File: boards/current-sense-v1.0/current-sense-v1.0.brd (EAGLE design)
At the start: 70.5 x 80.5 mm, 89 parts, among them IC1 ISO7241, IC2 ISO7241, IC3 ISO7242, IC4 ISO7240, J1 4-PIN_2MM-H, J2 MKS-1658, J3 8-PIN_2MM-H, J6 DF22-2, Q1 IRFH7545, Q2 IRFH7545, Q3 IRFH7545, Q4 IRFH7545, Q5 IRFH7545, Q6 IRFH7545, U1 DRV8303DCA, U13 TLV70233DBVR, U2 INA240PWR, U3 INA240PWR, U4 INA240PWR, U6 ADS8028IRTJT, U7 MPM3620GQV-P, U8 VND5E006ASPTR-E, U9 TLV70450

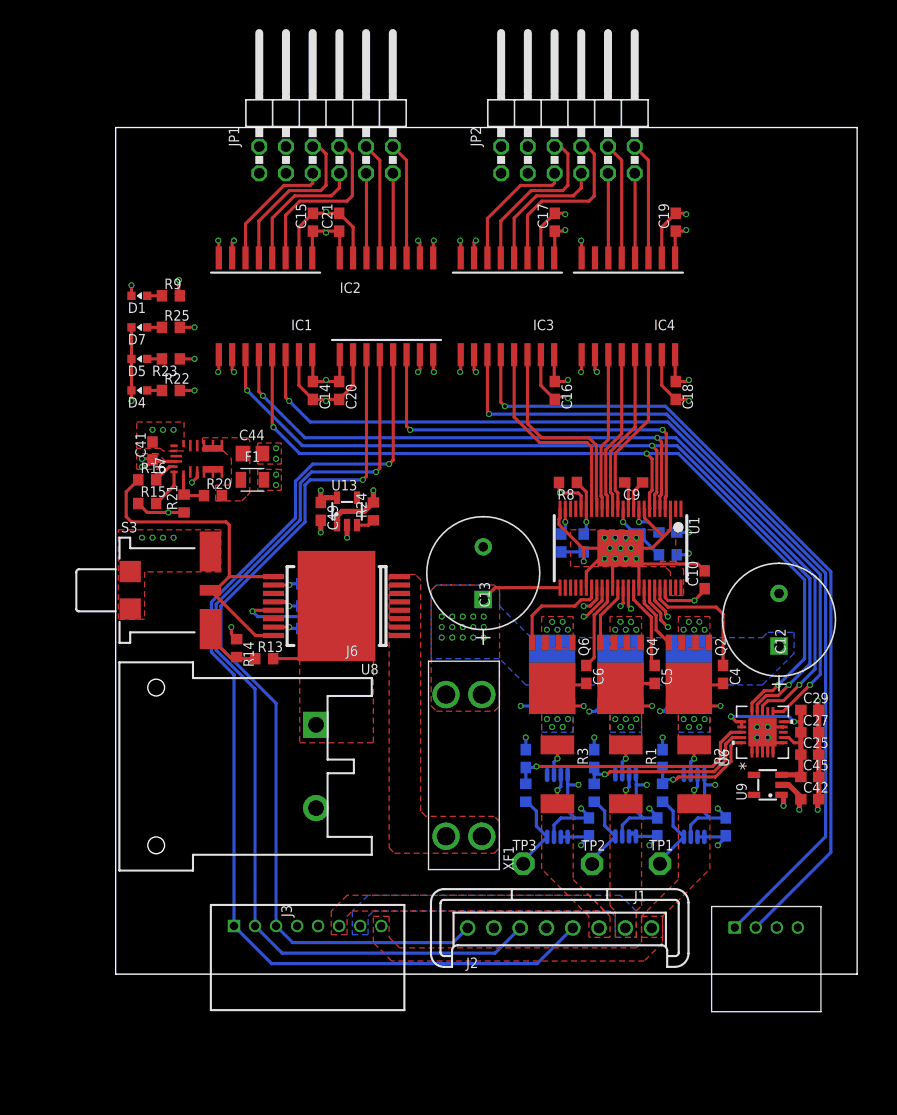
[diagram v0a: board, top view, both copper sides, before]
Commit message: Silkscreen fixes
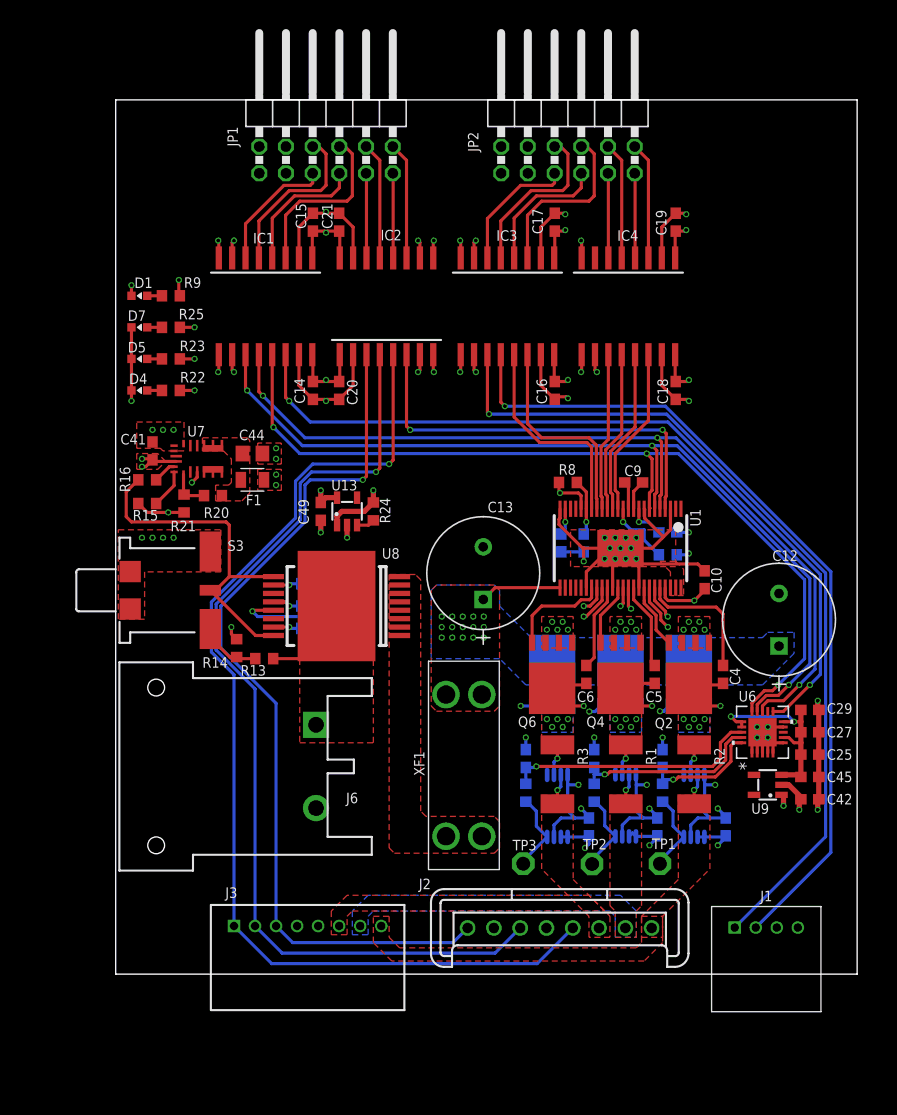
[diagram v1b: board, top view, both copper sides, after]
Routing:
- net +18.5V: track 29.0 -> 17.4 mm
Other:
- board size 70.5 x 80.5 mm -> 70.5 x 83.1 mm

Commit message: rotated the LDO
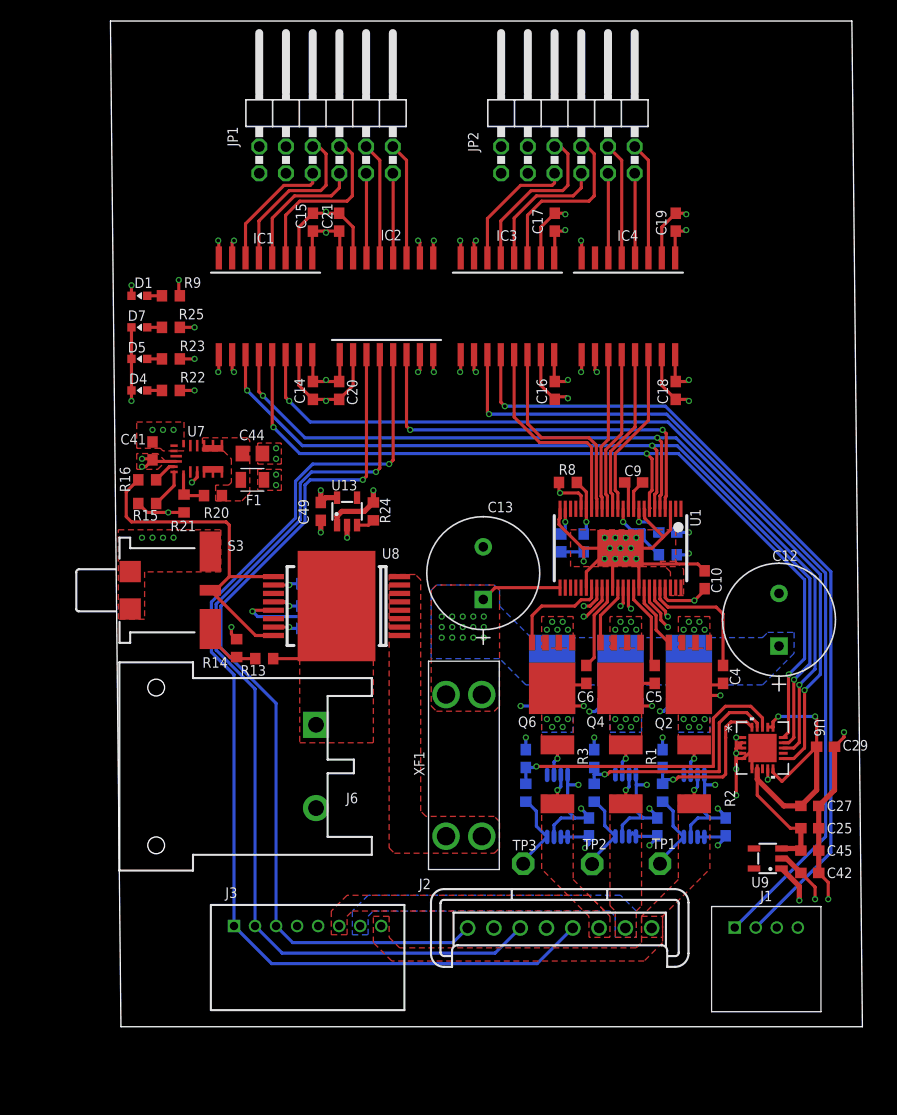
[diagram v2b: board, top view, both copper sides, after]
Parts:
- moved C25 7.00 mm to (66.0, 13.9)
- moved C27 7.00 mm to (66.0, 16.0)
- moved C42 7.00 mm to (66.0, 9.62)
- moved C45 7.00 mm to (66.0, 11.8)
- moved U9 7.00 mm to (62.0, 11.0)
- moved C29 3.81 mm to (67.5, 21.6)
- moved U6 1.50 mm to (61.5, 21.5), turned to 0 degrees
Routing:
- net ADC_5V: track 19.8 -> 35.4 mm, vias 2 -> 1
- net GND: track 183.3 -> 195.8 mm
- net SENSE_C: track 24.3 -> 30.5 mm
- net SENSE_B: track 17.9 -> 23.0 mm
- net CS_ADC: track 77.3 -> 81.4 mm
- net SENSE_A: track 11.4 -> 15.2 mm
- net N$3: track 0.00 -> 3.47 mm, vias 0 -> 1
- net MOSI: track 86.4 -> 88.8 mm
- net +18.5V: track 17.4 -> 19.3 mm
- net MISO: track 86.0 -> 87.6 mm
- net SH_A: track 28.3 -> 26.9 mm
- net SCK: track 84.1 -> 84.9 mm
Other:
- board size 70.5 x 83.1 mm -> 71.5 x 95.6 mm

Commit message: removed two ground symbols from board
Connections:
- net GND: no longer S3.LEG1, S3.LEG3
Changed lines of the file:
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@@
 <contactref element="U8" pad="13"/>
 <contactref element="R14" pad="1"/>
-<contactref element="S3" pad="LEG1"/>
-<contactref element="S3" pad="LEG3"/>
 <contactref element="S3" pad="3"/>
 <contactref element="D4" pad="C"/>
@@
 <wire x1="50.3" y1="43.3507375" x2="52" y2="41.6507375" width="0.3" layer="1"/>
 <wire x1="62" y1="18.5" x2="62.000125" y2="18.500125" width="0.1524" layer="1"/>
-<wire x1="44.305" y1="58.9" x2="51.925" y2="58.9" width="0" layer="19" extent="1-1"/>
-<wire x1="43" y1="54.75" x2="44.25" y2="57.25" width="0" layer="19" extent="1-1"/>
-<wire x1="32.805" y1="58.9" x2="40.425" y2="58.9" width="0" layer="19" extent="1-1"/>
-<wire x1="30.25" y1="57.25" x2="32.75" y2="57.25" width="0" layer="19" extent="1-1"/>
-<wire x1="22.575" y1="58.9" x2="30.195" y2="58.9" width="0" layer="19" extent="1-1"/>
-<wire x1="15.25" y1="50" x2="18.75" y2="54.65" width="0" layer="19" extent="1-1"/>
-<wire x1="15.25" y1="49" x2="15.25" y2="50" width="0" layer="19" extent="1-1"/>
-<wire x1="13.95" y1="49.5" x2="15.25" y2="50" width="0" layer="19" extent="1-1"/>
-<wire x1="7.75" y1="47.75" x2="13.95" y2="49.5" width="0" layer="19" extent="1-1"/>
-<wire x1="6.5" y1="43.9" x2="7.25" y2="46.75" width="0" layer="19" extent="1-1"/>
-<wire x1="5.5" y1="41.5" x2="5" y2="43.9" width="0" layer="19" extent="1-1"/>
-<wire x1="4.5" y1="41.5" x2="5.5" y2="41.5" width="0" layer="19" extent="1-1"/>
-<wire x1="3.5" y1="41.5" x2="4.5" y2="41.5" width="0" layer="19" extent="1-1"/>
-<wire x1="2.5" y1="41.5" x2="3.5" y2="41.5" width="0" layer="19" extent="1-1"/>
-<wire x1="5.55" y1="49.75" x2="7.75" y2="47.75" width="0" layer="19" extent="1-1"/>
-<wire x1="5.55" y1="50.25" x2="5.55" y2="49.75" width="0" layer="19" extent="1-1"/>
-<wire x1="6.45" y1="50.45" x2="5.55" y2="50.25" width="0" layer="19" extent="1-1"/>
-<wire x1="5.5" y1="51.75" x2="5.55" y2="50.25" width="0" layer="19" extent="1-1"/>
-<wire x1="4.5" y1="51.75" x2="5.5" y2="51.75" width="0" layer="19" extent="1-1"/>
-<wire x1="3.5" y1="51.75" x2="4.5" y2="51.75" width="0" layer="19" extent="1-1"/>
-<wire x1="3.5" y1="50.6" x2="3.5" y2="51.75" width="0" layer="19" extent="1-1"/>
-<wire x1="1.5" y1="54.5" x2="3.5" y2="51.75" width="0" layer="19" extent="1-1"/>
-<wire x1="1.38" y1="38.28" x2="2.5" y2="41.5" width="0" layer="19" extent="1-1"/>
-<wire x1="1.38" y1="34.72" x2="1.38" y2="38.28" width="0" layer="19" extent="1-1"/>
-<wire x1="9" y1="40.185" x2="5.5" y2="41.5" width="0" layer="19" extent="1-1"/>
-<wire x1="9.75" y1="57.25" x2="5.5" y2="51.75" width="0" layer="19" extent="1-1"/>
-<wire x1="13" y1="34.5" x2="9" y2="40.185" width="0" layer="19" extent="1-1"/>
-<wire x1="11" y1="33" x2="13" y2="34.5" width="0" layer="19" extent="1-1"/>
-<wire x1="19.5" y1="42" x2="19.35" y2="37.125" width="0" layer="19" extent="16-16"/>
-<wire x1="22" y1="41.5" x2="19.5" y2="42" width="0" layer="19" extent="1-1"/>
-<wire x1="52.75" y1="44.25" x2="54.5" y2="54.5" width="0" layer="19" extent="1-1"/>
-<wire x1="47" y1="40.5" x2="48" y2="40.5" width="0" layer="19" extent="1-1"/>
-<wire x1="53.35" y1="42" x2="52.75" y2="44.25" width="0" layer="19" extent="1-16"/>
-<wire x1="53.75" y1="36.75" x2="56" y2="38.35" width="0" layer="19" extent="1-1"/>
-<wire x1="53.25" y1="36.75" x2="53.75" y2="36.75" width="0" layer="19" extent="1-1"/>
-<wire x1="52.75" y1="36.75" x2="53.25" y2="36.75" width="0" layer="19" extent="1-1"/>
-<wire x1="54.5" y1="33.5" x2="53.75" y2="36.75" width="0" layer="19" extent="1-1"/>
-<wire x1="54" y1="32.75" x2="54.5" y2="33.5" width="0" layer="19" extent="1-1"/>
-<wire x1="55" y1="32.75" x2="54.5" y2="33.5" width="0" layer="19" extent="1-1"/>
-<wire x1="55.5" y1="33.5" x2="55" y2="32.75" width="0" layer="19" extent="1-1"/>
-<wire x1="56" y1="32.75" x2="55.5" y2="33.5" width="0" layer="19" extent="1-1"/>
-<wire x1="55.135" y1="31.52" x2="55" y2="32.75" width="0" layer="19" extent="1-1"/>
-<wire x1="53.865" y1="31.52" x2="54" y2="32.75" width="0" layer="19" extent="1-1"/>
-<wire x1="56.405" y1="31.52" x2="55.135" y2="31.52" width="0" layer="19" extent="1-1"/>
-<wire x1="49" y1="33.5" x2="49.75" y2="36.75" width="0" layer="19" extent="1-1"/>
-<wire x1="48.5" y1="32.75" x2="49" y2="33.5" width="0" layer="19" extent="1-1"/>
-<wire x1="48" y1="33.5" x2="48.5" y2="32.75" width="0" layer="19" extent="1-1"/>
-<wire x1="49.5" y1="32.75" x2="49" y2="33.5" width="0" layer="19" extent="1-1"/>
-<wire x1="47.5" y1="32.75" x2="48" y2="33.5" width="0" layer="19" extent="1-1"/>
-<wire x1="48.635" y1="31.52" x2="48.5" y2="32.75" width="0" layer="19" extent="1-1"/>
-<wire x1="47.365" y1="31.52" x2="47.5" y2="32.75" width="0" layer="19" extent="1-1"/>
-<wire x1="49.905" y1="31.52" x2="48.635" y2="31.52" width="0" layer="19" extent="1-1"/>
-<wire x1="43.405" y1="31.52" x2="47.365" y2="31.52" width="0" layer="19" extent="1-1"/>
-<wire x1="42.135" y1="31.52" x2="43.405" y2="31.52" width="0" layer="19" extent="1-1"/>
-<wire x1="42" y1="32.75" x2="42.135" y2="31.52" width="0" layer="19" extent="1-1"/>
-<wire x1="41.5" y1="33.5" x2="42" y2="32.75" width="0" layer="19" extent="1-1"/>
-<wire x1="42.5" y1="33.5" x2="42" y2="32.75" width="0" layer="19" extent="1-1"/>
-<wire x1="43" y1="32.75" x2="42.5" y2="33.5" width="0" layer="19" extent="1-1"/>
-<wire x1="41" y1="32.75" x2="41.5" y2="33.5" width="0" layer="19" extent="1-1"/>
-<wire x1="40.865" y1="31.52" x2="41" y2="32.75" width="0" layer="19" extent="1-1"/>
-<wire x1="63.07" y1="36.2" x2="56" y2="38.35" width="0" layer="19" extent="1-1"/>
-<wire x1="34.95" y1="40.63" x2="42.375" y2="40.15" width="0" layer="19" extent="16-16"/>
-<wire x1="52" y1="22.5" x2="53.865" y2="31.52" width="0" layer="19" extent="1-1"/>
-<wire x1="49.465003125" y1="19.000003125" x2="52" y2="21.35" width="0" layer="19" extent="16-16"/>
-<wire x1="45" y1="14.85" x2="48.165003125" y2="13.1" width="0" layer="19" extent="16-16"/>
-<wire x1="45.5" y1="21.35" x2="42.975003125" y2="18.950003125" width="0" layer="19" extent="16-16"/>
-<wire x1="54.675003125" y1="13.05" x2="51.5" y2="14.85" width="0" layer="19" extent="16-16"/>
-<wire x1="59" y1="17" x2="57" y2="18" width="0" layer="19" extent="1-1"/>
-<wire x1="60.499746875" y1="19.525" x2="59" y2="17" width="0" layer="19" extent="1-1"/>
-<wire x1="59" y1="17" x2="60.499746875" y2="19.525" width="0" layer="19" extent="1-1"/>
-<wire x1="59.62" y1="20.5" x2="59" y2="21" width="0" layer="19" extent="1-1"/>
+<wire x1="61.456621875" y1="22.043378125" x2="61.5" y2="21.5" width="0" layer="19" extent="1-1"/>
+<wire x1="59.525" y1="21" x2="59.525" y2="20.5" width="0" layer="19" extent="1-1"/>
+<wire x1="62.5" y1="22" x2="61.456621875" y2="22.043378125" width="0" layer="19" extent="1-1"/>
 <wire x1="62.000125" y1="19.525" x2="60.499746875" y2="19.525" width="0" layer="19" extent="1-1"/>
-<wire x1="39" y1="21.35" x2="42.975003125" y2="18.950003125" width="0" layer="19" extent="16-16"/>
-<wire x1="69.25" y1="23" x2="62.5" y2="22" width="0" layer="19" extent="1-1"/>
-<wire x1="65" y1="7" x2="67.75" y2="7.125" width="0" layer="19" extent="1-1"/>
-<wire x1="62.86" y1="4.43" x2="65" y2="7" width="0" layer="19" extent="1-1"/>
-<wire x1="35.96" y1="4.39" x2="41.675003125" y2="13.05" width="0" layer="19" extent="16-16"/>
-<wire x1="19.05" y1="15.79" x2="19.35" y2="32.875" width="0" layer="19" extent="16-16"/>
-<wire x1="17.25" y1="4.58" x2="19.05" y2="15.79" width="0" layer="19" extent="1-1"/>
-<wire x1="61.5" y1="21.5" x2="59" y2="17" width="0" layer="19"/>
 </signal>
 <signal name="PHASE_A">
@@
 <wire x1="64.5" y1="22.5" x2="64" y2="22" width="0.3" layer="1"/>
 <wire x1="64" y1="22" x2="63.475" y2="22" width="0.3" layer="1"/>
-<wire x1="64.475" y1="22.5" x2="64.475" y2="22" width="0" layer="19" extent="1-1"/>
+<wire x1="64.475" y1="22.5" x2="64.5" y2="22.5" width="0" layer="19" extent="1-1"/>
 </signal>
 <signal name="VBATT">

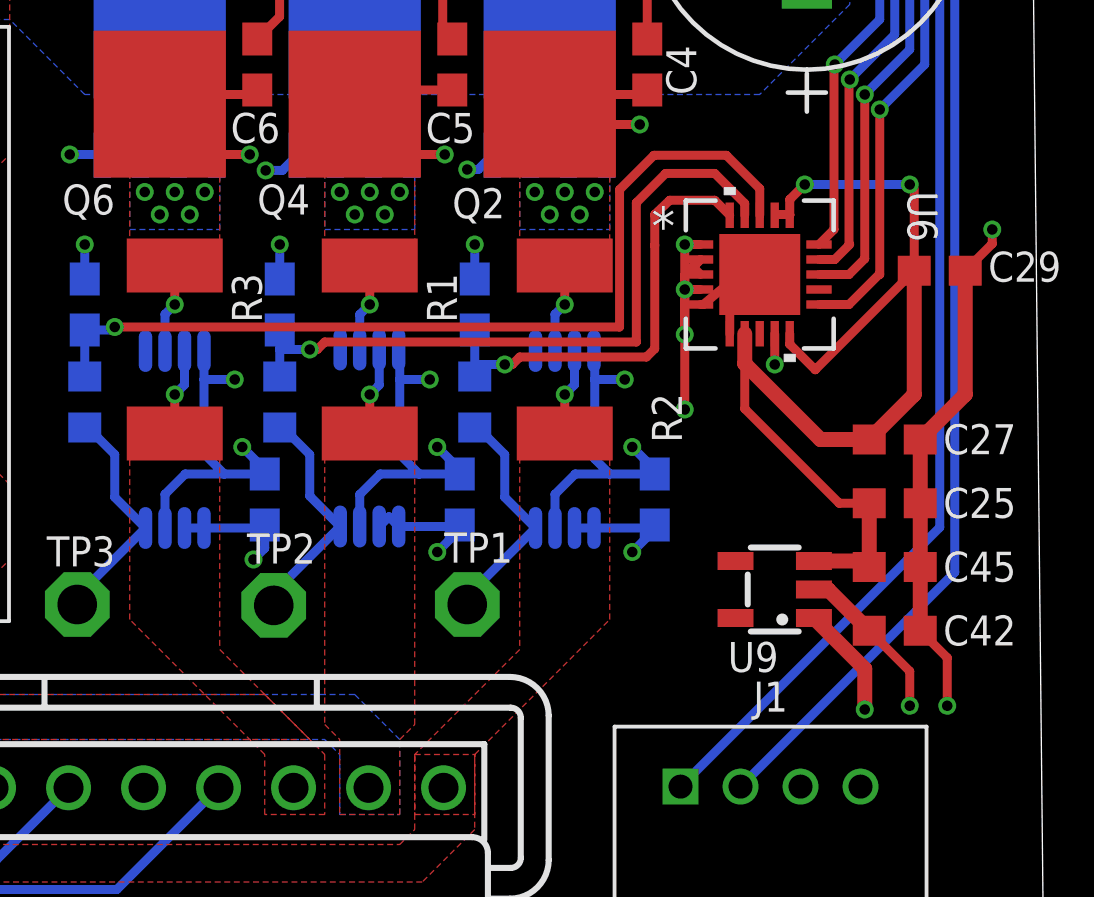
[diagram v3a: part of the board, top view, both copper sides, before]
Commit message: changed supply voltage of opamps to 3V3
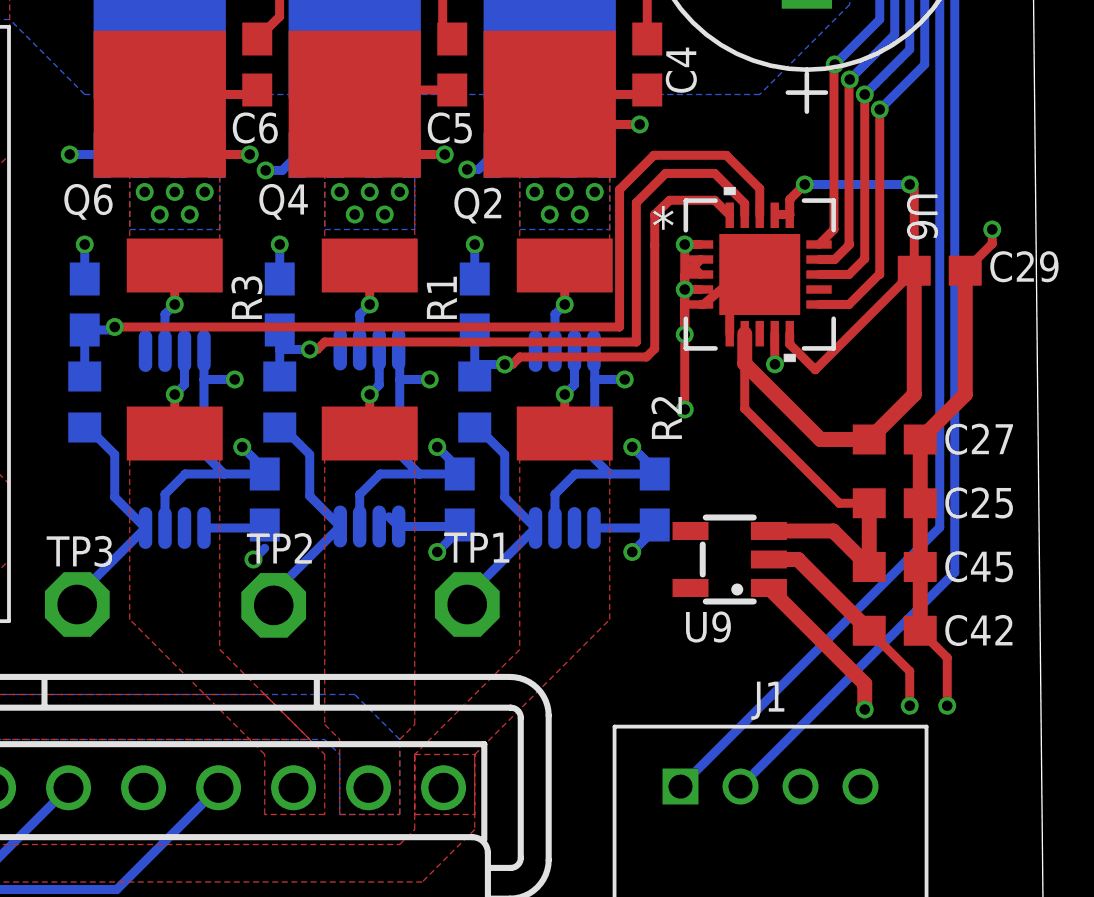
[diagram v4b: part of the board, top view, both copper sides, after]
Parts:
- moved U9 1.80 mm to (60.5, 12.0)
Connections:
- net ADC_5V renamed ADC_3V3
- net +3V3: now also C1.2, C2.2, C3.2, U2.5, U2.6, U3.5, U3.6, U4.5, U4.6
- net +5V: no longer C1.2, C2.2, C3.2, U2.5, U2.6, U3.5, U3.6, U4.5, U4.6
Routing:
- net +5V: track 158.7 -> 149.2 mm
- net +3V3: track 150.4 -> 157.0 mm
- net ADC_3V3: track 35.4 -> 40.8 mm, vias 1 -> 2
- net N$3: track 3.47 -> 0.00 mm, vias 1 -> 0
- net +18.5V: track 19.3 -> 21.2 mm
- net GND: track 195.8 -> 197.4 mm, vias 67 -> 68
